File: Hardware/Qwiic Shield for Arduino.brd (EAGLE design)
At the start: 53.3 x 59.7 mm, 104 parts, among them J1 Qwiic Right Angle, J10 Qwiic Right Angle, J8 Qwiic Right Angle, J9 Qwiic Right Angle, Q1 BSS138, Q2 BSS138, U1 ARDUINO UNO

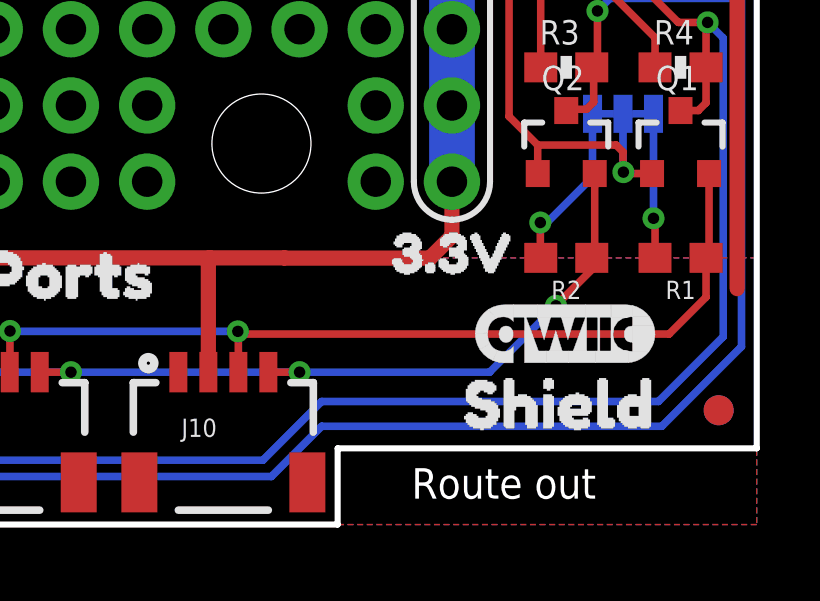
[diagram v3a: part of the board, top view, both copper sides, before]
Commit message: moved via away from qwiic silk logo
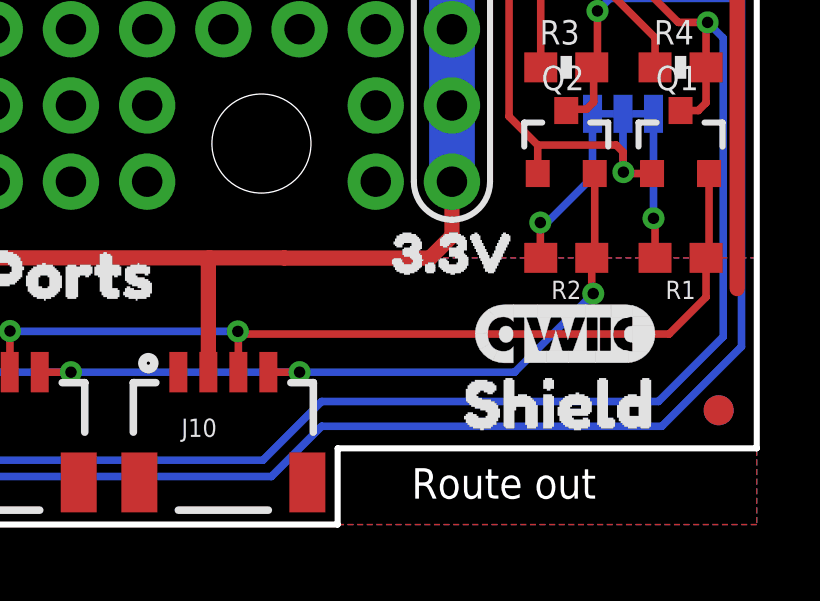
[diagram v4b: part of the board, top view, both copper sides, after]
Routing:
- net SCL: track 41.4 -> 42.0 mm
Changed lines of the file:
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@@
 <wire x1="47.94" y1="11.7" x2="47.94" y2="8.99" width="0.254" layer="1"/>
 <wire x1="47.94" y1="8.99" x2="47.84" y2="8.89" width="0.254" layer="1"/>
-<wire x1="47.84" y1="8.89" x2="47.84" y2="8.4954" width="0.254" layer="1"/>
 <wire x1="14.2" y1="5.08" x2="15.24" y2="5.08" width="0.254" layer="1"/>
 <via x="15.24" y="5.08" extent="1-16" drill="0.381"/>
@@
 <wire x1="38.1" y1="5.08" x2="37.108" y2="5.08" width="0.254" layer="1"/>
 <wire x1="37.108" y1="5.08" x2="37.084" y2="5.104" width="0.254" layer="1"/>
-<wire x1="47.84" y1="8.4954" x2="46.6471" y2="7.3025" width="0.254" layer="1"/>
-<wire x1="46.6471" y1="7.2898" x2="46.6471" y2="7.3025" width="0.254" layer="1"/>
-<via x="46.6471" y="7.2898" extent="1-16" drill="0.381"/>
-<wire x1="46.6471" y1="7.2898" x2="44.4373" y2="5.08" width="0.254" layer="16"/>
-<wire x1="44.4373" y1="5.08" x2="38.1" y2="5.08" width="0.254" layer="16"/>
+<wire x1="47.84" y1="8.89" x2="47.84" y2="7.7479" width="0.254" layer="1"/>
+<wire x1="47.889159375" y1="7.698740625" x2="47.84" y2="7.7479" width="0.254" layer="1"/>
+<via x="47.889159375" y="7.698740625" extent="1-16" drill="0.381"/>
+<wire x1="47.889159375" y1="7.698740625" x2="45.27041875" y2="5.08" width="0.254" layer="16"/>
+<wire x1="45.27041875" y1="5.08" x2="38.1" y2="5.08" width="0.254" layer="16"/>
 </signal>
 <signal name="SDA">
